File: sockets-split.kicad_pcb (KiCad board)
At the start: 2 copper layers, 63 parts, among them J2 MJ-4PP-9, P1 i2c-pin, P2 i2c-pin, SW1 RESET_SW, SW10 SW_PUSH, SW11 SW_PUSH, SW12 SW_PUSH, SW13 SW_PUSH, SW14 SW_PUSH, SW15 SW_PUSH, SW16 SW_PUSH, SW17 SW_PUSH, SW18 SW_PUSH, SW19 SW_PUSH, SW2 SW_PUSH, SW20 SW_PUSH, SW21 SW_PUSH, SW22 SW_PUSH, SW23 SW_PUSH, SW24 SW_PUSH, SW25 SW_PUSH, SW3 SW_PUSH, SW4 SW_PUSH, SW5 SW_PUSH, SW6 SW_PUSH, SW7 SW_PUSH, SW8 SW_PUSH, SW9 SW_PUSH, U1 ProMicro

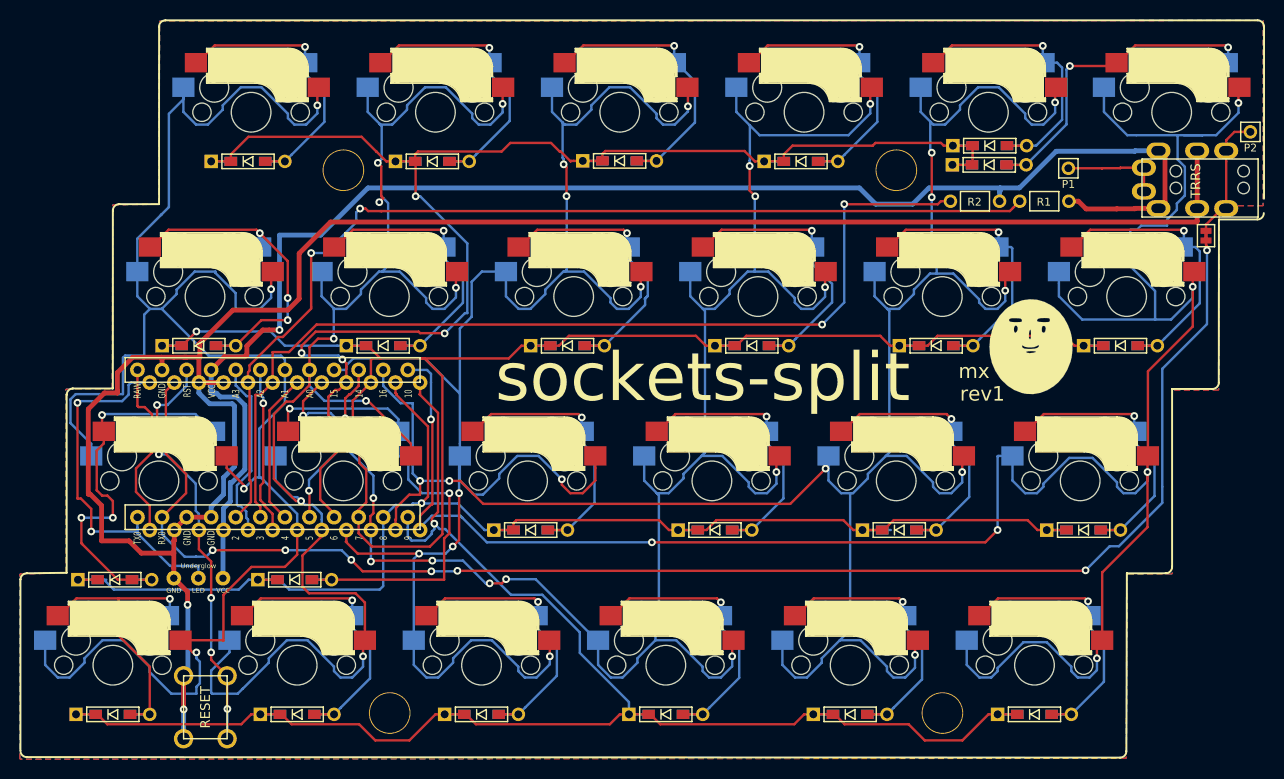
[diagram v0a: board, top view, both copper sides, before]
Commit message: Update docs]
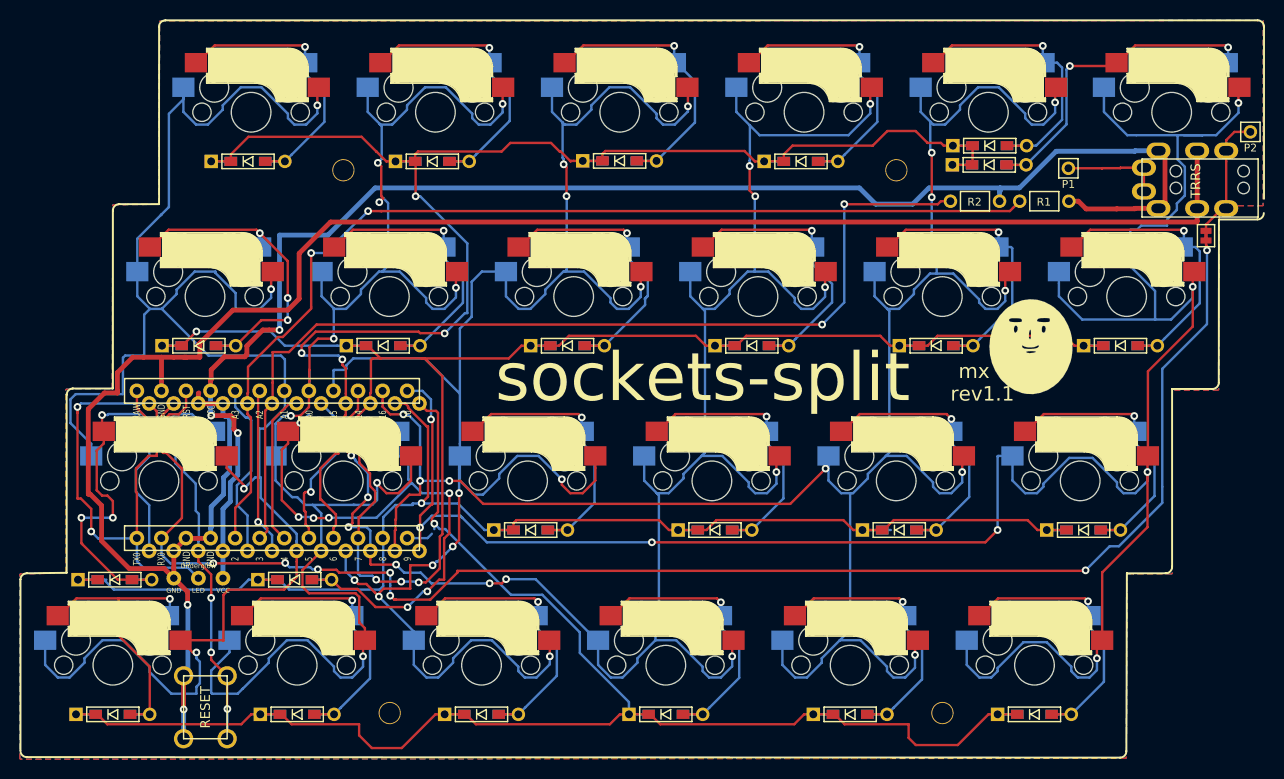
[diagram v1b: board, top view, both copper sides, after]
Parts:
- moved U1 2.16 mm to (117.5, 97.9)
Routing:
- net LED: track 38.4 -> 52.0 mm
- net Net-(D14-Pad2): track 50.7 -> 63.7 mm, vias 2 -> 7
- net row1: track 164.6 -> 172.9 mm, vias 1 -> 4
- net col2: track 181.3 -> 186.2 mm, vias 9 -> 11
- net col1: track 164.4 -> 159.7 mm
- net GND: track 210.0 -> 205.4 mm
- net RESET: track 43.5 -> 40.1 mm, vias 5 -> 4
- net Net-(U1-Pad8): track 19.9 -> 16.8 mm, vias 2 -> 1
- net data: track 155.4 -> 158.1 mm
- net row0: track 163.4 -> 166.0 mm
- net col0: track 186.0 -> 187.7 mm
- net SDA: track 107.4 -> 108.9 mm
- net row2: track 143.1 -> 141.7 mm
- net SCL: track 100.8 -> 102.2 mm
- net row3: track 168.6 -> 167.3 mm
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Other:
- board text added: "rev1.1"
- board text removed: "rev1"

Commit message: add docs images, fix pcb
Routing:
- net row3: track 167.3 -> 167.9 mm
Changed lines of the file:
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@@
     (thickness 1.6)
     (drawings 162)
-    (tracks 1646)
+    (tracks 1648)
     (zones 0)
     (modules 63)
@@
   (segment (start 126.0348 125.8648) (end 127.35 127.18) (width 0.25) (layer F.Cu) (net 23))
   (segment (start 127.35 127.18) (end 130.4435 127.18) (width 0.25) (layer F.Cu) (net 23))
+  (segment (start 133.5532 104.807285) (end 133.8072 104.553285) (width 0.25) (layer B.Cu) (net 23))
+  (segment (start 133.5532 105.037562) (end 133.5532 104.807285) (width 0.25) (layer B.Cu) (net 23))
   (segment (start 121.409 123.698) (end 123.444 123.698) (width 0.25) (layer B.Cu) (net 24))
   (segment (start 123.444 123.698) (end 121.409 123.698) (width 0.25) (layer F.Cu) (net 24))

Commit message: Update docs
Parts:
- removed the ? at (124.4, 67.8)
- removed the ? at (181.9, 67.7)
- removed the ? at (186.3, 124.1)
- removed the ? at (129.4, 124.5)
- added Ref**: Val**, kbd:HOLE, F.Cu at (126.0, 66.6)
- added Ref**: Val**, kbd:HOLE, F.Cu at (183.2, 66.7)
- added Ref**: Val**, kbd:HOLE, F.Cu at (189.6, 121.7)
- added Ref**: Val**, kbd:HOLE, F.Cu at (132.4, 121.8)
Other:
- board outline added: 128.5 x 76.2 mm
- board text added: "rev1.2"
- board text removed: "rev1.1"

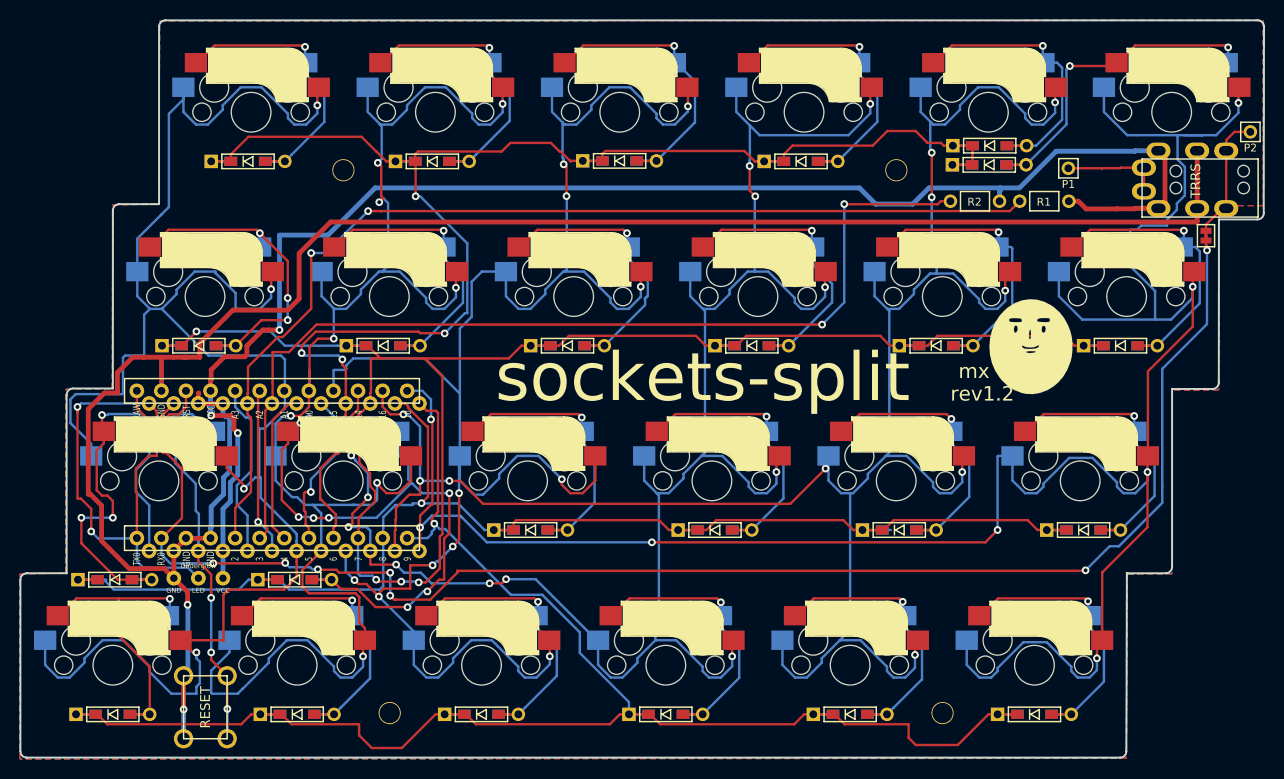
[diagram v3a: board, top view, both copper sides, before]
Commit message: promicroを変更
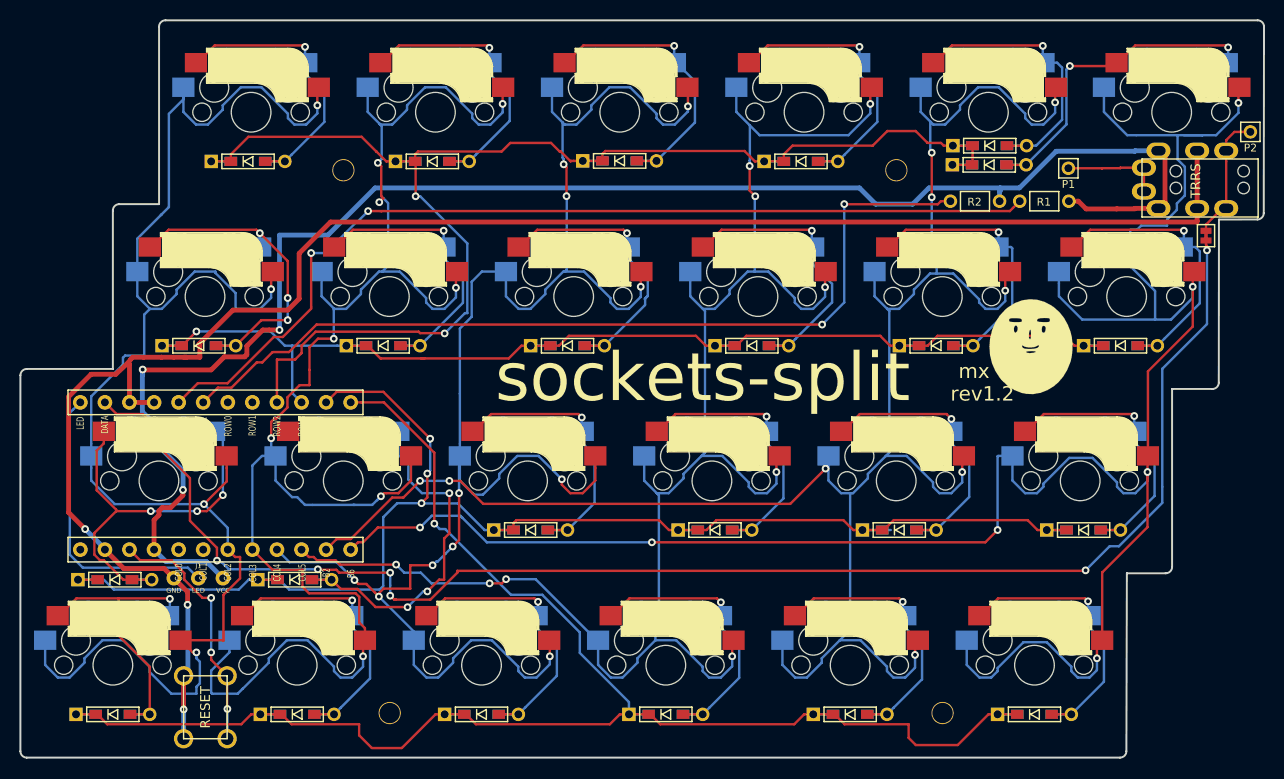
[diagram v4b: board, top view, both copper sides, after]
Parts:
- JP1: renamed from ?; value (none) -> Jumper_NC_Small
- U1: footprint kbd:ProMicro_v2_ura_pcb_for_sockets_split -> kbd:ProMicro_v2_1side
- moved U1 5.96 mm to (111.7, 99.1)
- renumbered Underglow to J1
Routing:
- net row1: track 172.9 -> 120.9 mm, vias 4 -> 1
- net col0: track 187.7 -> 161.1 mm
- net Net-(D14-Pad2): track 63.7 -> 38.1 mm, vias 7 -> 3
- net LED: track 52.0 -> 30.5 mm, vias 2 -> 0
- net GND: track 205.4 -> 185.6 mm, vias 2 -> 3
- net Net-(U1-Pad20): track 18.5 -> 0.00 mm
- net Net-(U1-Pad24): track 18.5 -> 0.00 mm, vias 1 -> 0
- net row0: track 166.0 -> 148.0 mm, vias 4 -> 2
- net Net-(U1-Pad19): track 17.8 -> 0.00 mm, vias 1 -> 0
- net Net-(U1-Pad8): track 16.8 -> 0.00 mm, vias 1 -> 0
- net Net-(U1-Pad7): track 15.9 -> 0.00 mm
- net col3: track 188.6 -> 173.9 mm, vias 12 -> 9
- net RESET: track 40.1 -> 26.2 mm, vias 4 -> 3
- net VCC: track 157.9 -> 170.8 mm
- net col2: track 186.2 -> 173.9 mm
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- removed copper zone on B.Cu, net (none)
- removed copper zone on F.Cu, net (none)
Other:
- outline, holes or cut-outs redrawn

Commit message: Add GNDベタ
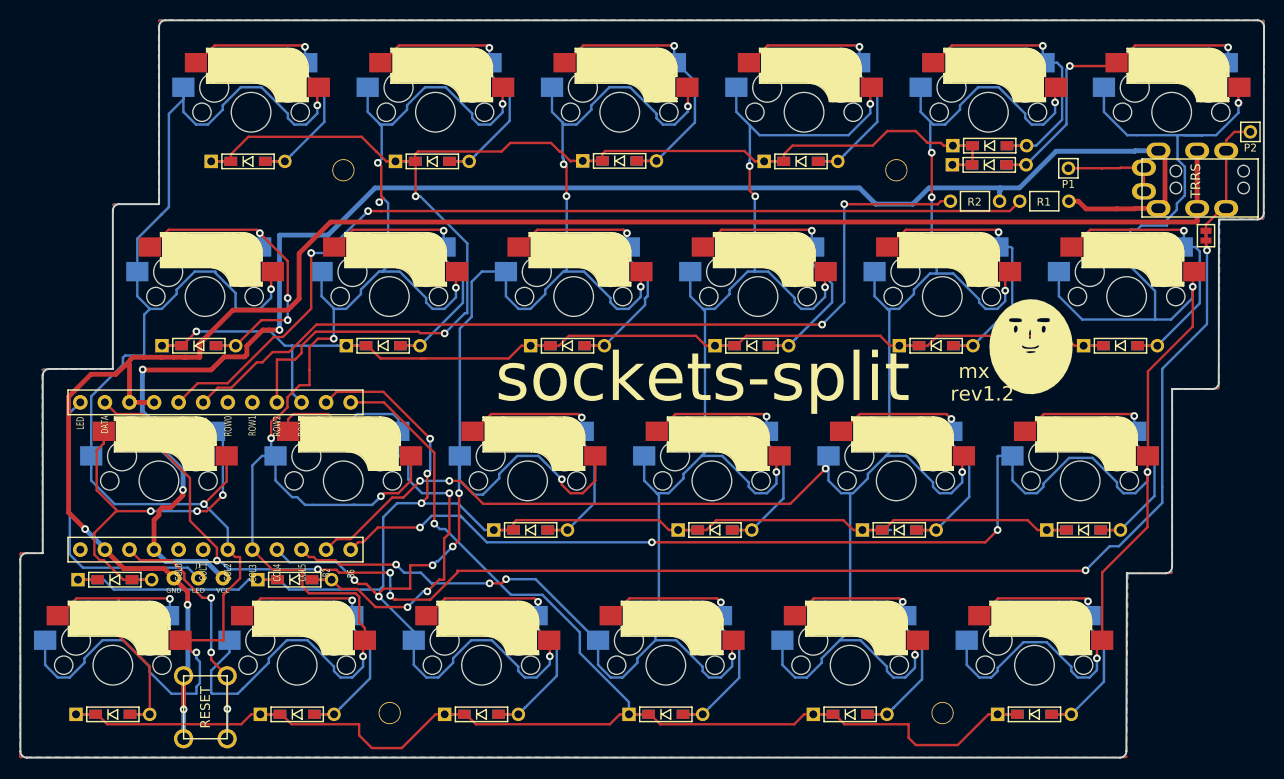
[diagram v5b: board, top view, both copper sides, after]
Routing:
- net Net-(D14-Pad2): track 38.1 -> 53.6 mm, vias 3 -> 4
- added copper zone on B.Cu, net (none)
- added copper zone on F.Cu, net (none)
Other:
- outline, holes or cut-outs redrawn
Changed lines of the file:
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@@
   (general
     (thickness 1.6)
-    (drawings 159)
-    (tracks 1401)
+    (drawings 162)
+    (tracks 1410)
     (zones 0)
     (modules 63)
@@
     (pad "" np_thru_hole circle (at -3.2429 1.7824) (size 2.3 2.3) (drill 2.1) (layers *.Cu *.Mask))
   )
-  (gr_line (start 100.58 88) (end 91.69 88) (layer Edge.Cuts) (width 0.2))
+  (gr_line (start 91.68 107.04) (end 93.34 107.04) (layer Edge.Cuts) (width 0.2))
+  (gr_arc (start 91.68 107.7004) (end 91.68 107.04) (angle -90) (layer Edge.Cuts) (width 0.2))
+  (gr_line (start 93.339682 107.039601) (end 93.339682 88.650001) (layer Edge.Cuts) (width 0.2))
+  (gr_line (start 100.58 88) (end 94 88) (layer Edge.Cuts) (width 0.2))
   (gr_circle (center 109.8296 122.9092) (end 111.3296 122.9092) (layer Dwgs.User) (width 0.2))
   (gr_line (start 101.4478 47.4986) (end 101.4478 67.056) (layer Dwgs.User) (width 0.2))
@@
   (gr_arc (start 106.0196 52.6288) (end 106.0196 51.9684) (angle -90) (layer Edge.Cuts) (width 0.2))
   (gr_arc (start 101.2444 71.628) (end 101.2444 70.9676) (angle -90) (layer Edge.Cuts) (width 0.2))
-  (gr_arc (start 91.6904 88.6604) (end 91.6904 88) (angle -89.09777884) (layer Edge.Cuts) (width 0.2))
+  (gr_arc (start 94 88.6604) (end 94 88) (angle -89.09777884) (layer Edge.Cuts) (width 0.2))
   (gr_arc (start 204.6732 127.508) (end 204.6732 128.1684) (angle -90) (layer Edge.Cuts) (width 0.2))
   (gr_arc (start 91.6904 127.51) (end 91.03 127.51) (angle -90) (layer Edge.Cuts) (width 0.2))
-  (gr_line (start 91.03 88.65) (end 91.03 127.51) (layer Edge.Cuts) (width 0.2))
+  (gr_line (start 91.0196 107.7004) (end 91.03 127.51) (layer Edge.Cuts) (width 0.2))
   (gr_line (start 100.584 71.628) (end 100.584 88) (layer Edge.Cuts) (width 0.2))
   (gr_line (start 105.3592 70.9676) (end 101.2444 70.9676) (layer Edge.Cuts) (width 0.2))
@@
   (segment (start 132.483151 101.872757) (end 129.972843 101.872757) (width 0.25) (layer B.Cu) (net 16))
   (segment (start 128.160899 110.802301) (end 118.803501 110.802301) (width 0.25) (layer B.Cu) (net 16))
+  (segment (start 125.837001 92.662999) (end 124.34 94.16) (width 0.25) (layer B.Cu) (net 17))
+  (segment (start 129.561499 92.662999) (end 125.837001 92.662999) (width 0.25) (layer B.Cu) (net 17))
+  (via (at 124.34 94.16) (size 0.8) (drill 0.4) (layers F.Cu B.Cu) (net 17))
+  (segment (start 130.0965 94.448) (end 130.0965 93.198) (width 0.25) (layer B.Cu) (net 17))
+  (segment (start 130.0965 93.198) (end 129.561499 92.662999) (width 0.25) (layer B.Cu) (net 17))
+  (segment (start 122.842999 92.662999) (end 119.231501 92.662999) (width 0.25) (layer F.Cu) (net 17))
+  (segment (start 118.6965 93.198) (end 118.6965 94.448) (width 0.25) (layer F.Cu) (net 17))
+  (segment (start 119.231501 92.662999) (end 118.6965 93.198) (width 0.25) (layer F.Cu) (net 17))
+  (segment (start 124.34 94.16) (end 122.842999 92.662999) (width 0.25) (layer F.Cu) (net 17))
   (segment (start 128.597102 91.4536) (end 126.23963 91.4536) (width 0.25) (layer F.Cu) (net 23))
   (segment (start 133.8072 96.663698) (end 128.597102 91.4536) (width 0.25) (layer F.Cu) (net 23))
@@
   (segment (start 215.25 71.4) (end 213.5632 73.0868) (width 0.25) (layer F.Cu) (net 48))
   (segment (start 215.65 71.4) (end 215.25 71.4) (width 0.25) (layer F.Cu) (net 48))
+  (zone (net 0) (net_name "") (layer F.Cu) (hatch edge 0.508)
+    (connect_pads (clearance 0.508))
+    (min_thickness 0.254)
+    (fill yes (arc_segments 32) (thermal_gap 0.508) (thermal_bridge_width 0.508))
+    (polygon
+      (pts
+        (xy 219.54 72.51) (xy 214.94 72.56) (xy 214.87 90.04) (xy 210.09 90.06) (xy 210.04 109.1)
+        (xy 205.47 109.1) (xy 205.38 128.16) (xy 90.97 128.18) (xy 90.98 107.01) (xy 93.32 107.02)
+        (xy 93.3 88.04) (xy 100.56 87.97) (xy 100.59 70.98) (xy 105.33 70.99) (xy 105.31 51.98)
+        (xy 219.54 51.97)
+      )
+    )
+  )
+  (zone (net 0) (net_name "") (layer B.Cu) (hatch edge 0.508)
+    (connect_pads (clearance 0.508))
+    (min_thickness 0.254)
+    (fill yes (arc_segments 32) (thermal_gap 0.508) (thermal_bridge_width 0.508))
+    (polygon
+      (pts
+        (xy 219.56 51.96) (xy 219.55 72.49) (xy 215 72.51) (xy 214.9 90.05) (xy 210.1 90.03)
+        (xy 210.08 109.1) (xy 205.49 109.14) (xy 205.34 128.13) (xy 90.95 128.11) (xy 91.01 107.03)
+        (xy 93.32 107.03) (xy 93.27 88.02) (xy 100.59 88) (xy 100.61 70.96) (xy 105.32 70.96)
+        (xy 105.31 51.93)
+      )
+    )
+  )
 )
